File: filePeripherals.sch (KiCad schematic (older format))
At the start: 18 parts, among them J2 PP1_receptacle_TE_5-5530843-4, J3 PP1_receptacle_TE_5-5530843-4, J4 PP1_receptacle_TE_5-5530843-4, J5 PP1_receptacle_TE_5-5530843-4, U6 CD74AC238, U7 74AHC138

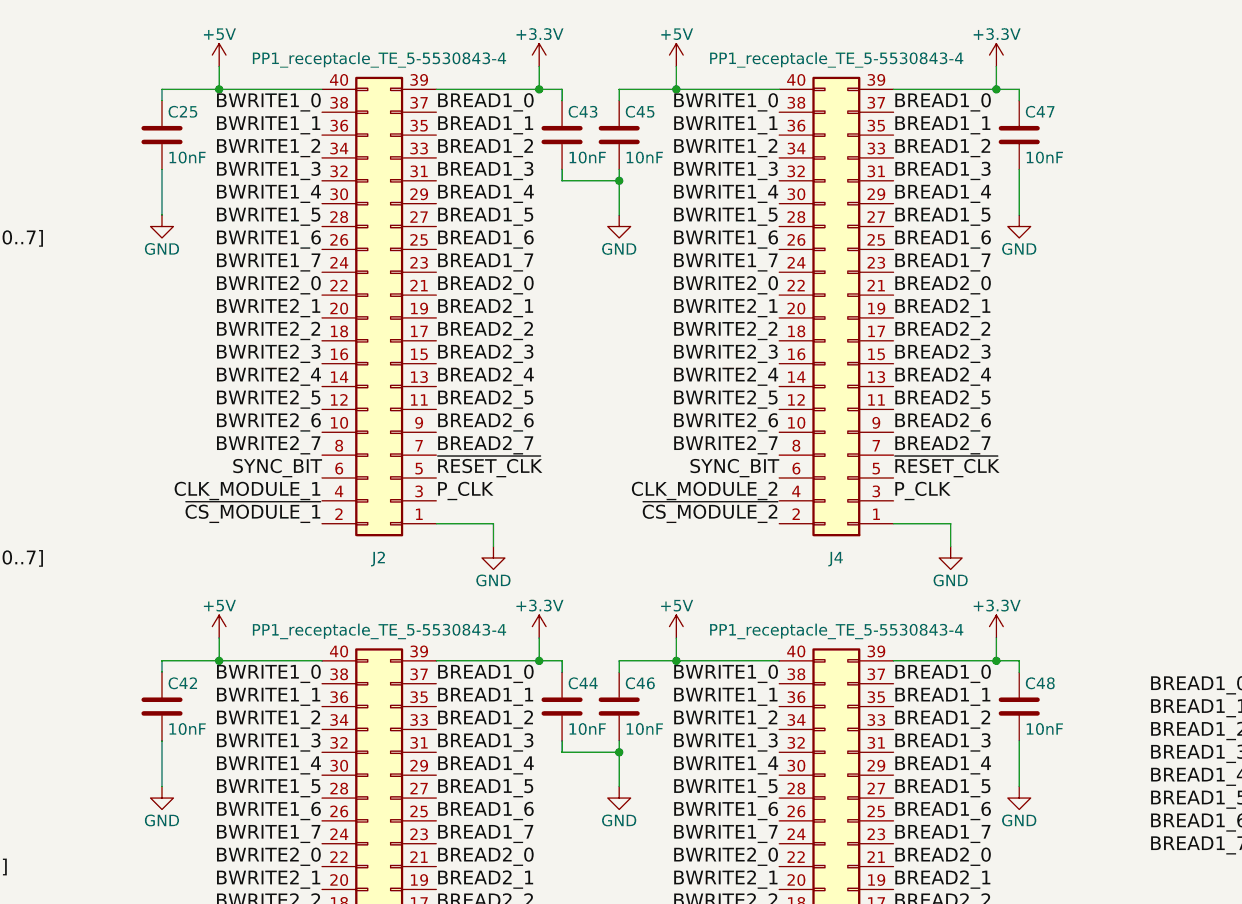
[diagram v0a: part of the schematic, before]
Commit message: Better decoupling
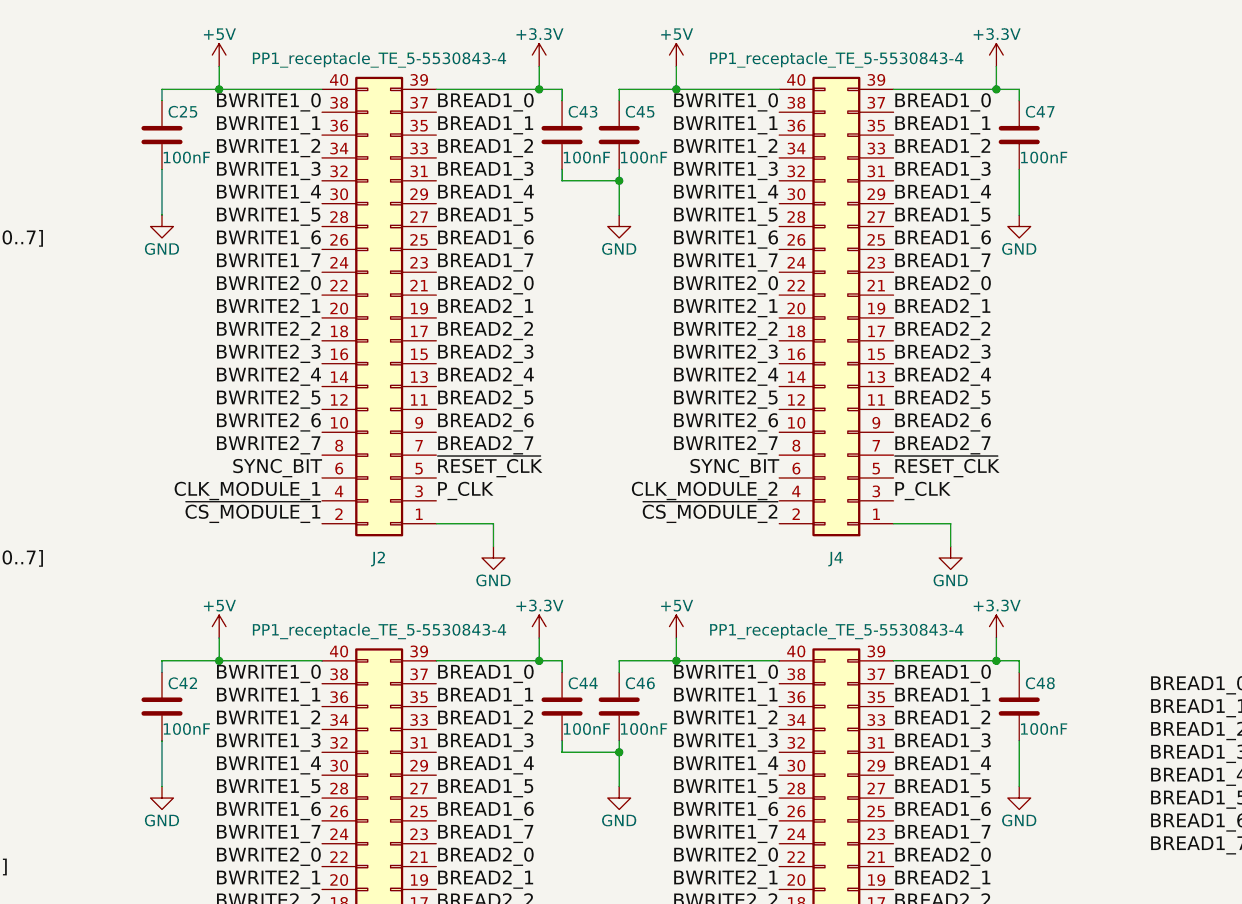
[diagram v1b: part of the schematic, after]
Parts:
- C25, C42, C43, C44, C45, C46, C47, C48: value 10nF -> 100nF
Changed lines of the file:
@@
 AR Path="/5A97A24B/5C7994AC" Ref="C48"  Part="1"
 F 0 "C48" H 6525 3700 50  0000 L CNN
-F 1 "10nF" H 6525 3500 50  0000 L CNN
+F 1 "100nF" H 6500 3500 50  0000 L CNN
 F 2 "Capacitor_SMD:C_0805_2012Metric" H 6538 3450 50  0001 C CNN
 F 3 "" H 6500 3600 50  0001 C CNN
@@
 AR Path="/5A97A24B/5C799628" Ref="C44"  Part="1"
 F 0 "C44" H 4525 3700 50  0000 L CNN
-F 1 "10nF" H 4525 3500 50  0000 L CNN
+F 1 "100nF" H 4500 3500 50  0000 L CNN
 F 2 "Capacitor_SMD:C_0805_2012Metric" H 4538 3450 50  0001 C CNN
 F 3 "" H 4500 3600 50  0001 C CNN
@@
 AR Path="/5A97A24B/5C7996BA" Ref="C46"  Part="1"
 F 0 "C46" H 4775 3700 50  0000 L CNN
-F 1 "10nF" H 4775 3500 50  0000 L CNN
+F 1 "100nF" H 4750 3500 50  0000 L CNN
 F 2 "Capacitor_SMD:C_0805_2012Metric" H 4788 3450 50  0001 C CNN
 F 3 "" H 4750 3600 50  0001 C CNN
@@
 AR Path="/5A97A24B/5C799729" Ref="C42"  Part="1"
 F 0 "C42" H 2775 3700 50  0000 L CNN
-F 1 "10nF" H 2775 3500 50  0000 L CNN
+F 1 "100nF" H 2750 3500 50  0000 L CNN
 F 2 "Capacitor_SMD:C_0805_2012Metric" H 2788 3450 50  0001 C CNN
 F 3 "" H 2750 3600 50  0001 C CNN
@@
 AR Path="/5A97A24B/5C799DA9" Ref="C47"  Part="1"
 F 0 "C47" H 6525 1200 50  0000 L CNN
-F 1 "10nF" H 6525 1000 50  0000 L CNN
+F 1 "100nF" H 6500 1000 50  0000 L CNN
 F 2 "Capacitor_SMD:C_0805_2012Metric" H 6538 950 50  0001 C CNN
 F 3 "" H 6500 1100 50  0001 C CNN
@@
 AR Path="/5A97A24B/5C799F8A" Ref="C45"  Part="1"
 F 0 "C45" H 4775 1200 50  0000 L CNN
-F 1 "10nF" H 4775 1000 50  0000 L CNN
+F 1 "100nF" H 4750 1000 50  0000 L CNN
 F 2 "Capacitor_SMD:C_0805_2012Metric" H 4788 950 50  0001 C CNN
 F 3 "" H 4750 1100 50  0001 C CNN
@@
 AR Path="/5A97A24B/5C79A0DC" Ref="C43"  Part="1"
 F 0 "C43" H 4525 1200 50  0000 L CNN
-F 1 "10nF" H 4525 1000 50  0000 L CNN
+F 1 "100nF" H 4500 1000 50  0000 L CNN
 F 2 "Capacitor_SMD:C_0805_2012Metric" H 4538 950 50  0001 C CNN
 F 3 "" H 4500 1100 50  0001 C CNN
@@
 AR Path="/5A97A24B/5C79A155" Ref="C25"  Part="1"
 F 0 "C25" H 2775 1200 50  0000 L CNN
-F 1 "10nF" H 2775 1000 50  0000 L CNN
+F 1 "100nF" H 2750 1000 50  0000 L CNN
 F 2 "Capacitor_SMD:C_0805_2012Metric" H 2788 950 50  0001 C CNN
 F 3 "" H 2750 1100 50  0001 C CNN
